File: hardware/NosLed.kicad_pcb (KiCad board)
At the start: 2 copper layers, 35 x 100 mm, 65 parts, among them J101 USB_C_Receptacle_USB2.0_16P, J102 LOAD, J103 AC, U101 AMS1117-3.3, U102 ESP32-C3-WROOM-02U, U301 BP2876, U401 LNK306D, U501 BP2876

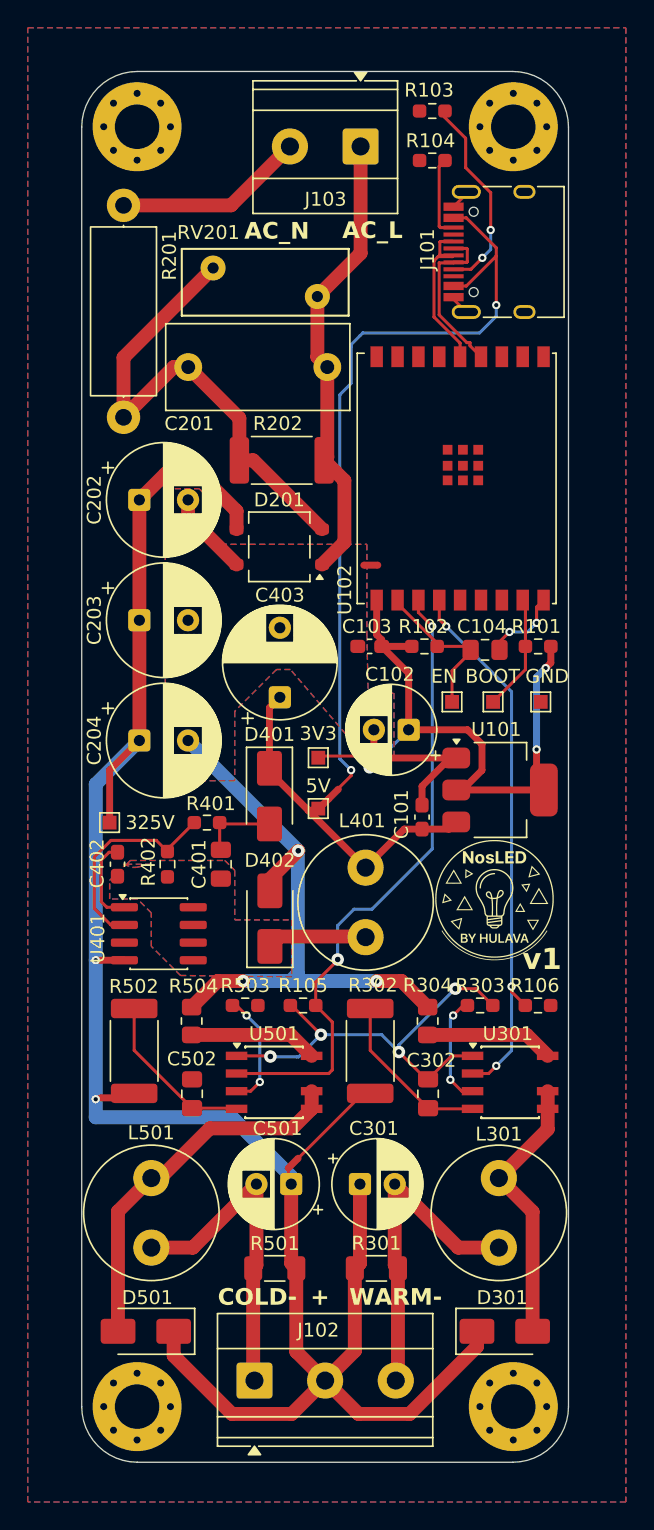
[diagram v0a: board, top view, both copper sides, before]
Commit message: Use non-hand soldering footprints
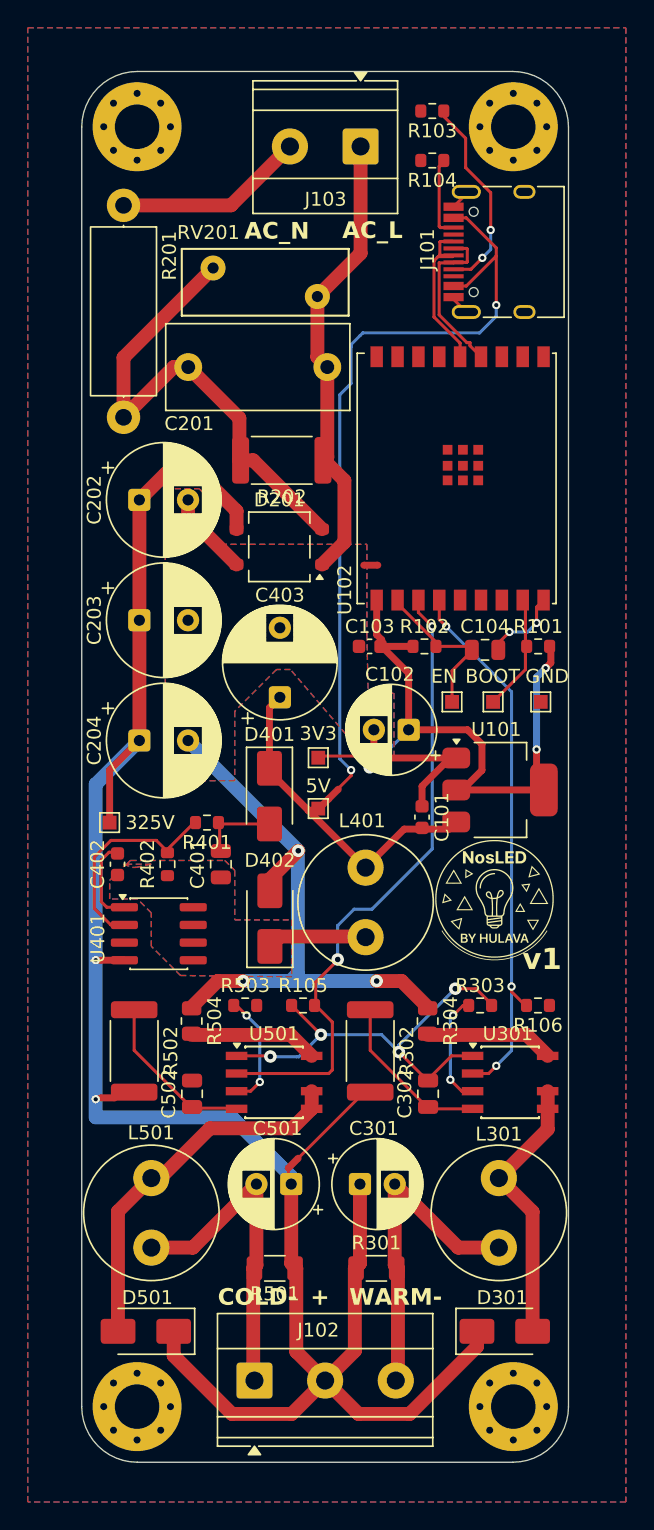
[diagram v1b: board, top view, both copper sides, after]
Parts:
- C101, C103, C402: footprint Capacitor_SMD:C_0603_1608Metric_Pad1.08x0.95mm_HandSolder -> Capacitor_SMD:C_0603_1608Metric
- C104, C302, C401, C502: footprint Capacitor_SMD:C_0805_2012Metric_Pad1.18x1.45mm_HandSolder -> Capacitor_SMD:C_0805_2012Metric
- R101, R102, R103, R104, R105, R106, R303, R401, R402, R503: footprint Resistor_SMD:R_0603_1608Metric_Pad0.98x0.95mm_HandSolder -> Resistor_SMD:R_0603_1608Metric
- R202, R302, R502: footprint Resistor_SMD:R_2512_6332Metric_Pad1.40x3.35mm_HandSolder -> Resistor_SMD:R_2512_6332Metric
- R301, R501: footprint Resistor_SMD:R_1206_3216Metric_Pad1.30x1.75mm_HandSolder -> Resistor_SMD:R_1206_3216Metric
- R304, R504: footprint Resistor_SMD:R_0805_2012Metric_Pad1.20x1.40mm_HandSolder -> Resistor_SMD:R_0805_2012Metric

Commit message: Hotfixes
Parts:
- C102: value 100uF 10V -> 220uF 25V
- C403: value 470uF 10V -> 470uF 16V
- L401: value 2.2mH -> 470uF
- R304, R504: value 2.7 -> 2R7
- U401: footprint Package_SO:SOIC-8_3.9x4.9mm_P1.27mm -> NosLib:LNK302PN-SOIC-8_3.9x4.9mm_P1.27mm
- turned D401 to 90 degrees
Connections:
- C401 pad 2: Net-(D401-A) -> Net-(D401-K)
- D401 pad 1: 5V -> Net-(D401-K)
- D401 pad 2: Net-(D401-A) -> 5V
- R401 pad 1: Net-(D401-A) -> Net-(D401-K)
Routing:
- net Net-(D401-K): track 0.00 -> 5.61 mm
- net Net-(D401-A): track 5.61 -> 0.00 mm
- net Net-(U501-ROVP): track 8.44 -> 10.7 mm
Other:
- board text added: "v1.0"
- board text removed: "v1"

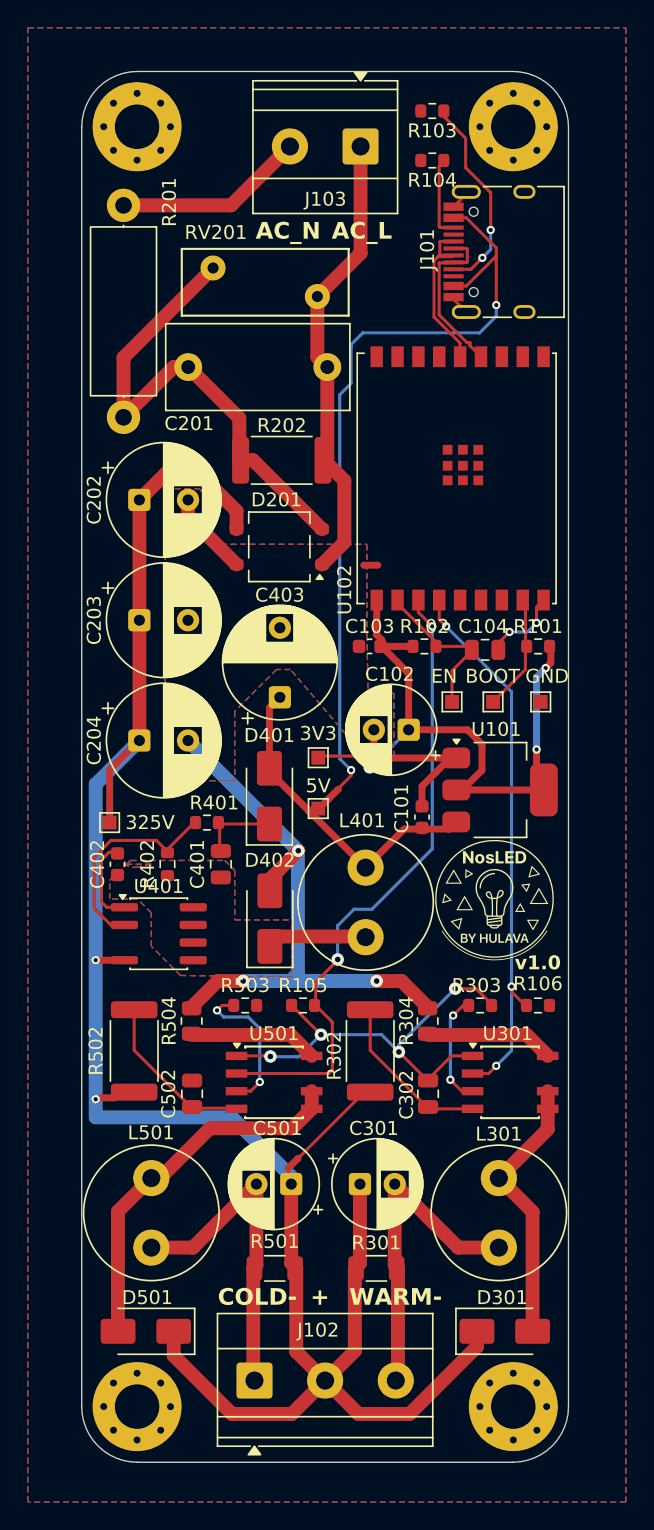
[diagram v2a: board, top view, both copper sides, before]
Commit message: Fix holes
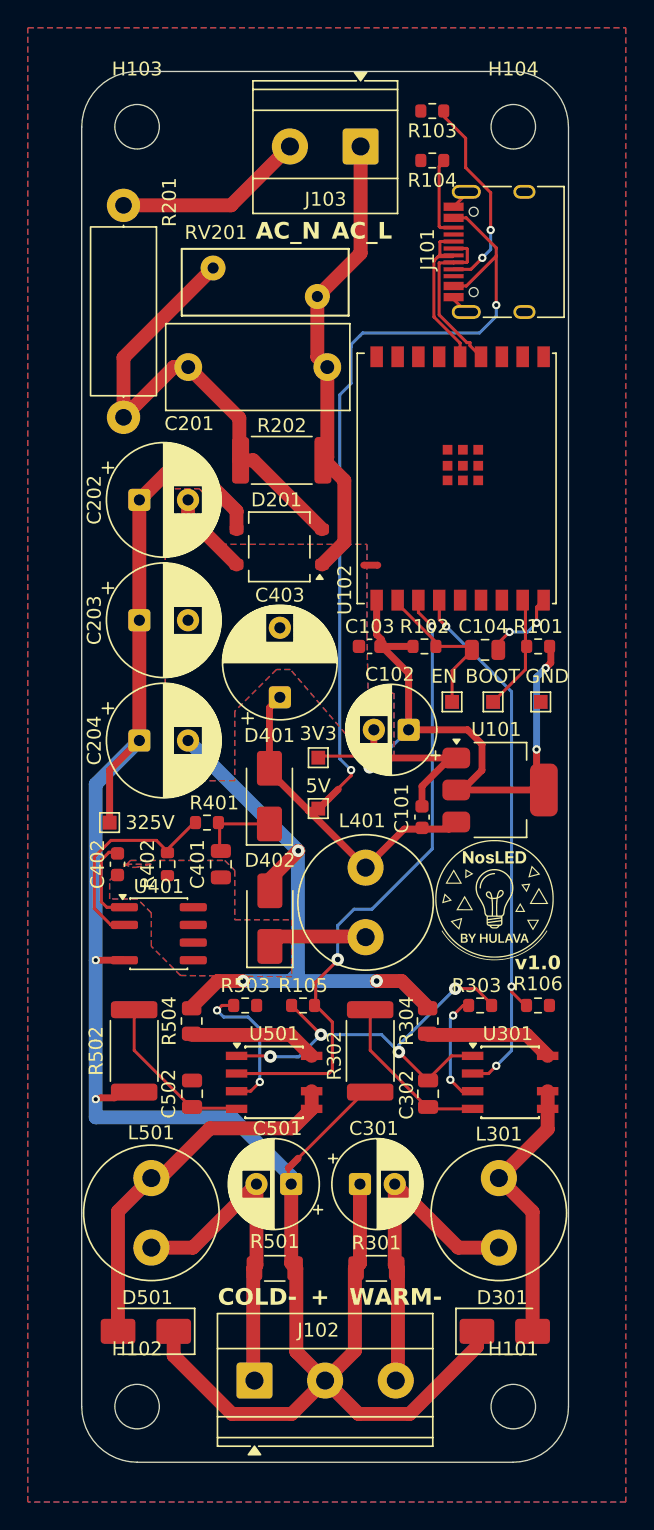
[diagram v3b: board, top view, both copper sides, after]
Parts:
- H101, H102, H103, H104: footprint MountingHole:MountingHole_3.2mm_M3_Pad_Via -> MountingHole:MountingHole_3.2mm_M3
